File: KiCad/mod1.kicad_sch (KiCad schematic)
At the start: 62 parts, among them M1 Fan_4pin, M2 Fan_4pin

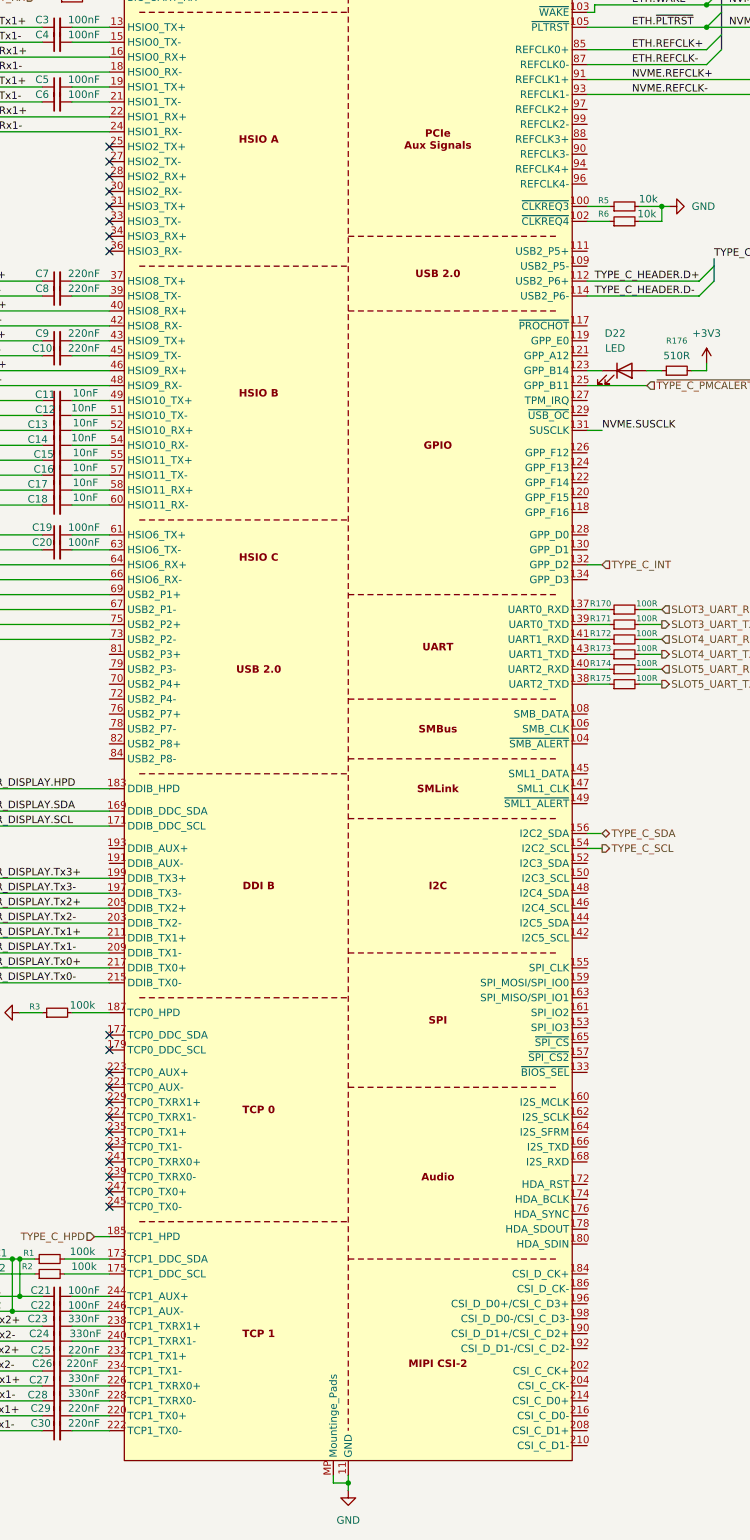
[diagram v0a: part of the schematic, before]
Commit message: Add programming header and power and reset switches
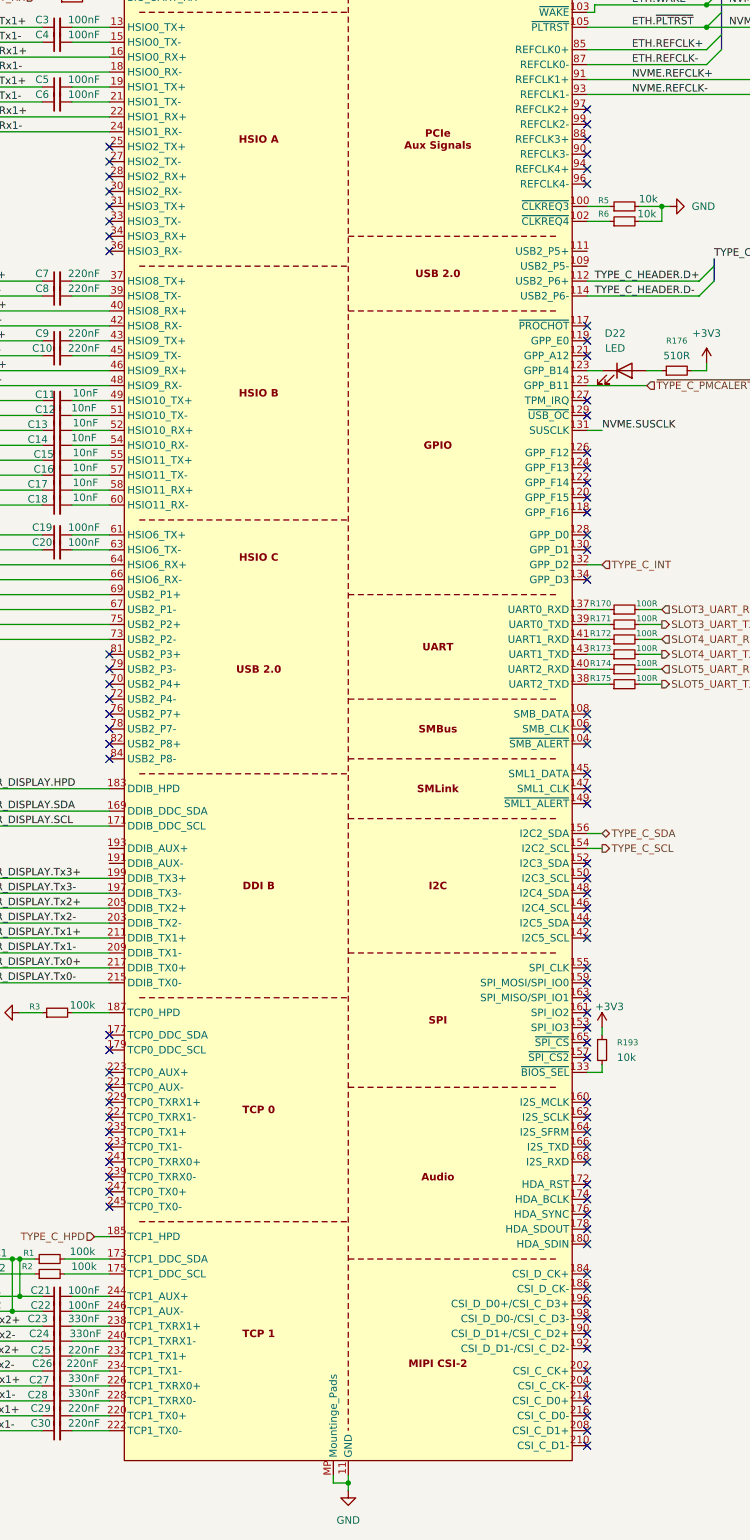
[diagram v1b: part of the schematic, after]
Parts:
- added R193: 10k, symbol Device:R_Small
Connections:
- net +3V3: now also R193.1
- net at A1.133 (~{BIOS_SEL}): now also R193.2
- no-connect marks 21 -> 89

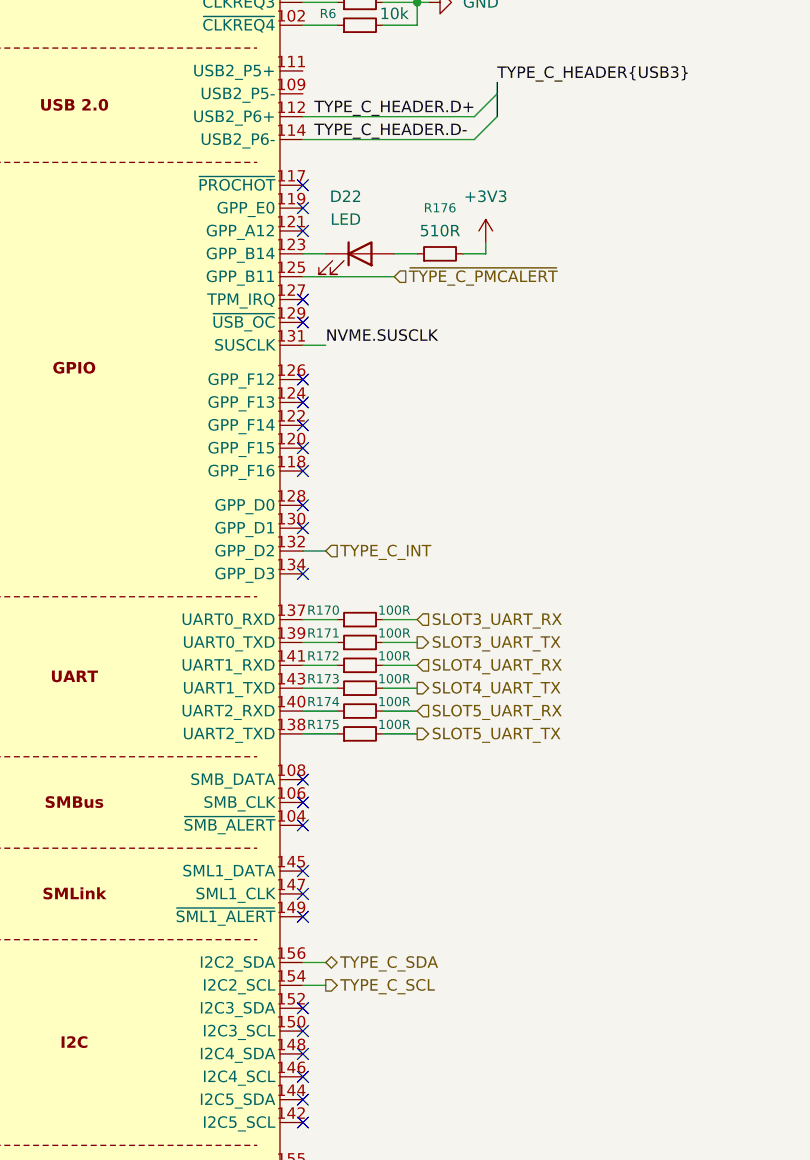
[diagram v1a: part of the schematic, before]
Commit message: Add TPS65987D PD controller, switch stm32 to cheaper one
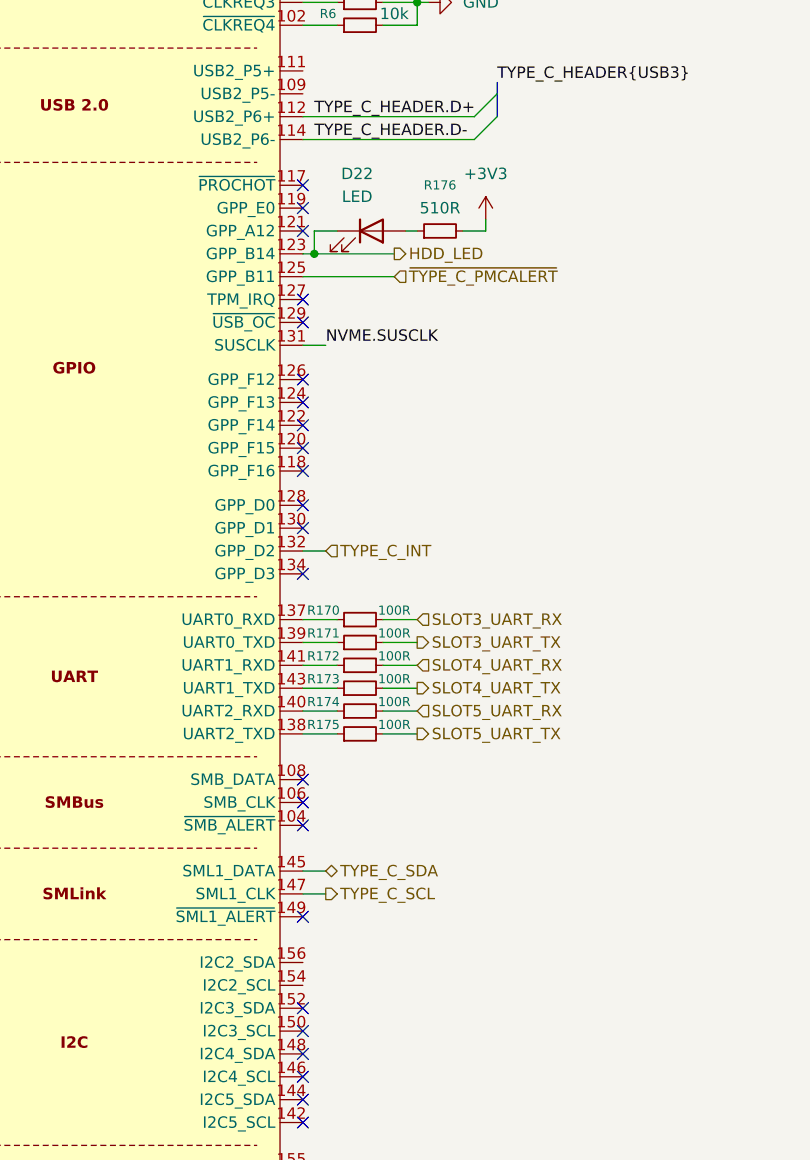
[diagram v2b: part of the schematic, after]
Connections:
- net TYPE_C_SCL: now also A1.147 (SML1_CLK); no longer A1.154 (I2C2_SCL)
- net TYPE_C_SDA: now also A1.145 (SML1_DATA); no longer A1.156 (I2C2_SDA)
- net HDD_LED: now reaches A1.123 (GPP_B14), D22.1 (K)
- no-connect marks 89 -> 87
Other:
- moved on the sheet: D22, R176
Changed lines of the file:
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@@
 	)
 	(junction
+		(at 326.39 156.21)
+		(diameter 0)
+		(color 0 0 0 0)
+	)
+	(junction
 		(at 403.86 52.07)
 		(diameter 0)
@@
 	)
 	(no_connect
-		(at 325.12 227.33)
-	)
-	(no_connect
 		(at 325.12 80.01)
 	)
@@
 	)
 	(no_connect
-		(at 325.12 224.79)
-	)
-	(no_connect
 		(at 243.84 290.83)
 	)
@@
 	(wire
 		(pts
+			(xy 326.39 156.21) (xy 325.12 156.21)
+		)
+		(stroke
+			(width 0)
+			(type default)
+		)
+	)
+	(wire
+		(pts
 			(xy 349.25 44.45) (xy 349.25 41.91)
 		)
@@
 	(wire
 		(pts
+			(xy 325.12 224.79) (xy 327.66 224.79)
+		)
+		(stroke
+			(width 0)
+			(type default)
+		)
+	)
+	(wire
+		(pts
 			(xy 237.49 323.85) (xy 243.84 323.85)
 		)
@@
 	(wire
 		(pts
-			(xy 345.44 154.94) (xy 345.44 156.21)
+			(xy 345.44 152.4) (xy 345.44 153.67)
 		)
 		(stroke
@@
 	(wire
 		(pts
-			(xy 345.44 156.21) (xy 342.9 156.21)
+			(xy 345.44 153.67) (xy 342.9 153.67)
 		)
 		(stroke
@@
 	(wire
 		(pts
-			(xy 325.12 156.21) (xy 327.66 156.21)
+			(xy 326.39 153.67) (xy 328.93 153.67)
 		)
 		(stroke
@@
 	(wire
 		(pts
+			(xy 326.39 156.21) (xy 335.28 156.21)
+		)
+		(stroke
+			(width 0)
+			(type default)
+		)
+	)
+	(wire
+		(pts
 			(xy 237.49 161.29) (xy 243.84 161.29)
 		)
@@
 	(wire
 		(pts
+			(xy 325.12 227.33) (xy 327.66 227.33)
+		)
+		(stroke
+			(width 0)
+			(type default)
+		)
+	)
+	(wire
+		(pts
 			(xy 325.12 201.93) (xy 328.93 201.93)
 		)
@@
 	(wire
 		(pts
+			(xy 326.39 153.67) (xy 326.39 156.21)
+		)
+		(stroke
+			(width 0)
+			(type default)
+		)
+	)
+	(wire
+		(pts
 			(xy 237.49 143.51) (xy 243.84 143.51)
 		)
@@
 	(wire
 		(pts
-			(xy 335.28 156.21) (xy 337.82 156.21)
-		)
-		(stroke
-			(width 0)
-			(type default)
-		)
-	)
-	(wire
-		(pts
-			(xy 325.12 234.95) (xy 327.66 234.95)
+			(xy 336.55 153.67) (xy 337.82 153.67)
 		)
 		(stroke
@@
 	(wire
 		(pts
-			(xy 325.12 237.49) (xy 327.66 237.49)
-		)
-		(stroke
-			(width 0)
-			(type default)
-		)
-	)
-	(wire
-		(pts
 			(xy 325.12 189.23) (xy 327.66 189.23)
 		)
@@
 		)
 	)
+	(hierarchical_label "HDD_LED"
+		(shape output)
+		(at 335.28 156.21 0)
+		(effects
+			(font
+				(size 1.27 1.27)
+			)
+			(justify left)
+		)
+	)
 	(hierarchical_label "SLOT2_UART_RX"
 		(shape input)
@@
 	(hierarchical_label "TYPE_C_SCL"
 		(shape output)
-		(at 327.66 237.49 0)
+		(at 327.66 227.33 0)
 		(effects
 			(font
@@
 	(hierarchical_label "TYPE_C_SDA"
 		(shape bidirectional)
-		(at 327.66 234.95 0)
+		(at 327.66 224.79 0)
 		(effects
 			(font
@@
 	(symbol
 		(lib_id "Device:LED")
-		(at 331.47 156.21 0)
+		(at 332.74 153.67 0)
 		(unit 1)
 		(exclude_from_sim no)
@@
 		(fields_autoplaced yes)
 		(property "Reference" "D22"
-			(at 329.8825 149.86 0)
+			(at 331.1525 147.32 0)
 			(effects
 				(font
@@
 		)
 		(property "Value" "LED"
-			(at 329.8825 152.4 0)
+			(at 331.1525 149.86 0)
 			(effects
 				(font
@@
 		)
 		(property "Footprint" ""
-			(at 331.47 156.21 0)
+			(at 332.74 153.67 0)
 			(effects
 				(font
@@
 		)
 		(property "Datasheet" "~"
-			(at 331.47 156.21 0)
+			(at 332.74 153.67 0)
 			(effects
 				(font
@@
 		)
 		(property "Description" "Light emitting diode"
-			(at 331.47 156.21 0)
+			(at 332.74 153.67 0)
 			(effects
 				(font
@@
 		)
 		(property "Sim.Pins" "1=K 2=A"
-			(at 331.47 156.21 0)
+			(at 332.74 153.67 0)
 			(effects
 				(font
@@
 	(symbol
 		(lib_id "Device:R_Small")
-		(at 340.36 156.21 90)
+		(at 340.36 153.67 90)
 		(unit 1)
 		(exclude_from_sim no)
@@
 		(fields_autoplaced yes)
 		(property "Reference" "R176"
-			(at 340.36 151.13 90)
+			(at 340.36 148.59 90)
 			(effects
 				(font
@@
 		)
 		(property "Value" "510R"
-			(at 340.36 153.67 90)
+			(at 340.36 151.13 90)
 			(effects
 				(font
@@
 		)
 		(property "Footprint" ""
-			(at 340.36 156.21 0)
+			(at 340.36 153.67 0)
 			(effects
 				(font
@@
 		)
 		(property "Datasheet" "~"
-			(at 340.36 156.21 0)
+			(at 340.36 153.67 0)
 			(effects
 				(font
@@
 		)
 		(property "Description" "Resistor, small symbol"
-			(at 340.36 156.21 0)
+			(at 340.36 153.67 0)
 			(effects
 				(font
@@
 	(symbol
 		(lib_id "power:+3V3")
-		(at 345.44 154.94 0)
+		(at 345.44 152.4 0)
 		(unit 1)
 		(exclude_from_sim no)
@@
 		(fields_autoplaced yes)
 		(property "Reference" "#PWR0209"
-			(at 345.44 158.75 0)
+			(at 345.44 156.21 0)
 			(effects
 				(font
@@
 		)
 		(property "Value" "+3V3"
-			(at 345.44 149.86 0)
+			(at 345.44 147.32 0)
 			(effects
 				(font
@@
 		)
 		(property "Footprint" ""
-			(at 345.44 154.94 0)
+			(at 345.44 152.4 0)
 			(effects
 				(font
@@
 		)
 		(property "Datasheet" ""
-			(at 345.44 154.94 0)
+			(at 345.44 152.4 0)
 			(effects
 				(font
@@
 		)
 		(property "Description" "Power symbol creates a global label with name \"+3V3\""
-			(at 345.44 154.94 0)
+			(at 345.44 152.4 0)
 			(effects
 				(font

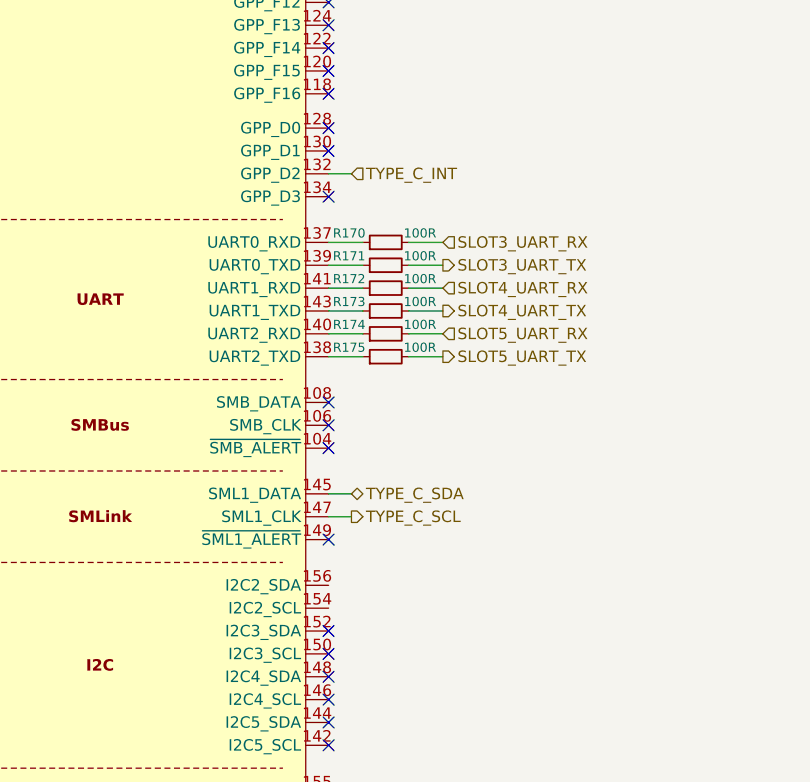
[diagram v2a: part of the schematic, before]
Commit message: Connect TPS65987D I2C and Interrupts
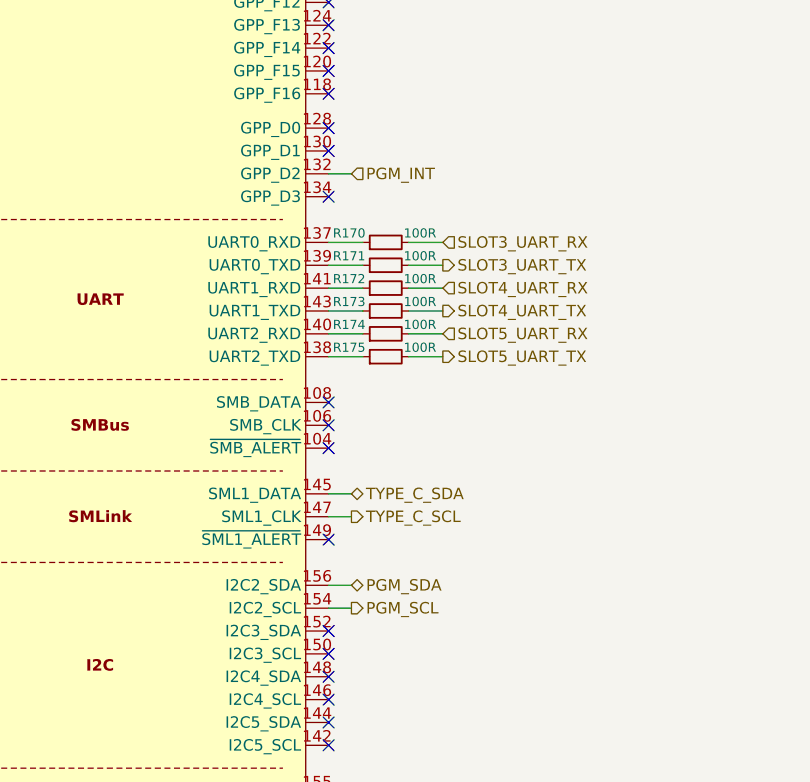
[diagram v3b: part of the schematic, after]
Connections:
- net PGM_SCL: now reaches A1.154 (I2C2_SCL)
- net PGM_SDA: now reaches A1.156 (I2C2_SDA)
- net TYPE_C_INT renamed PGM_INT
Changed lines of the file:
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@@
 	(wire
 		(pts
+			(xy 325.12 237.49) (xy 327.66 237.49)
+		)
+		(stroke
+			(width 0)
+			(type default)
+		)
+	)
+	(wire
+		(pts
 			(xy 212.09 309.88) (xy 218.44 309.88)
 		)
@@
 	(wire
 		(pts
+			(xy 325.12 234.95) (xy 327.66 234.95)
+		)
+		(stroke
+			(width 0)
+			(type default)
+		)
+	)
+	(wire
+		(pts
 			(xy 228.6 307.34) (xy 231.14 307.34)
 		)
@@
 		)
 	)
+	(hierarchical_label "PGM_SDA"
+		(shape bidirectional)
+		(at 327.66 234.95 0)
+		(effects
+			(font
+				(size 1.27 1.27)
+			)
+			(justify left)
+		)
+	)
 	(hierarchical_label "RUSB_1{USB3}"
 		(shape input)
@@
 		)
 	)
-	(hierarchical_label "TYPE_C_INT"
+	(hierarchical_label "PGM_INT"
 		(shape input)
 		(at 327.66 189.23 0)
 		(effects
 			(font
+				(size 1.27 1.27)
+			)
+			(justify left)
+		)
+	)
+	(hierarchical_label "PGM_SCL"
+		(shape output)
+		(at 327.66 237.49 0)
+		(effects
+			(font

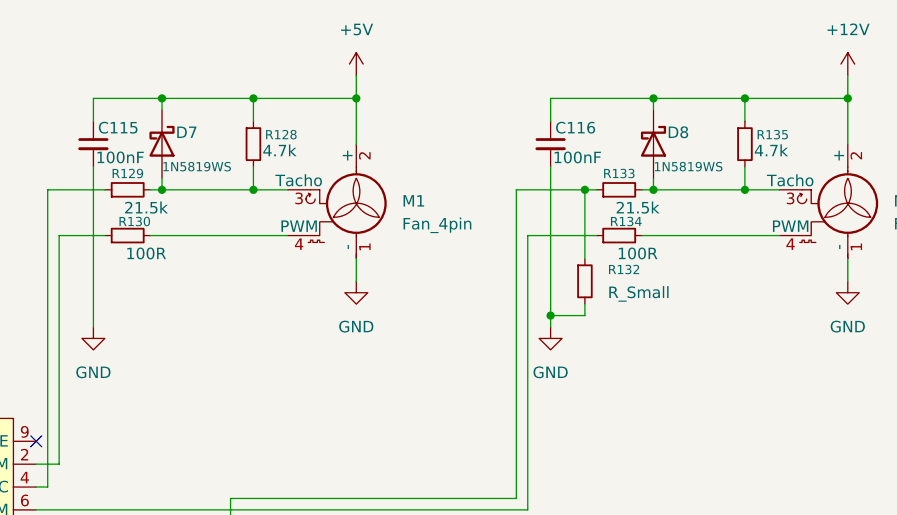
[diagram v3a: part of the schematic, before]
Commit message: Fix some diodes and resistors
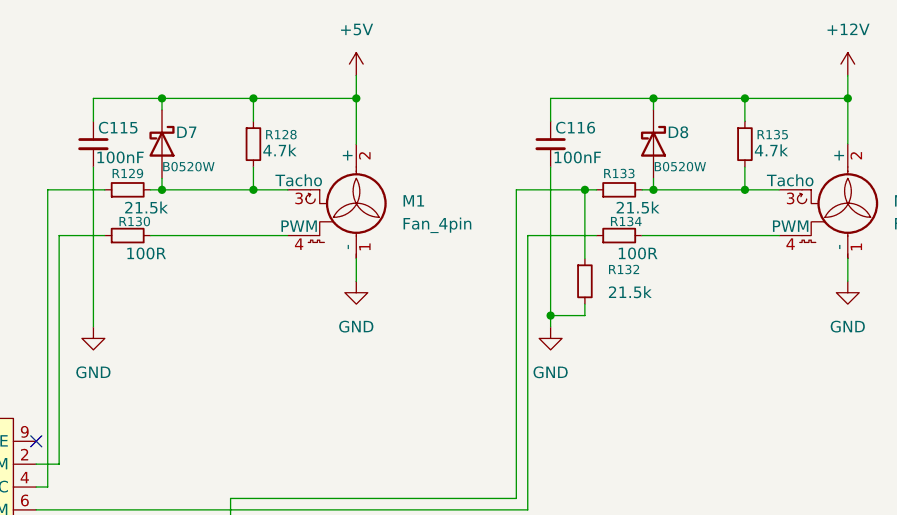
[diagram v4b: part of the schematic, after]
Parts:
- D7, D8: value 1N5819WS -> B0520W
- R132: value R_Small -> 21.5k
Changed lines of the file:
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@@
 			)
 		)
-		(property "Value" "1N5819WS"
+		(property "Value" "B0520W"
 			(at 339.09 49.53 90)
 			(effects
@@
 			)
 		)
-		(property "Value" "1N5819WS"
+		(property "Value" "B0520W"
 			(at 393.7 49.53 90)
 			(effects
@@
 			)
 		)
-		(property "Value" "R_Small"
+		(property "Value" "21.5k"
 			(at 388.62 63.4999 0)
 			(effects
